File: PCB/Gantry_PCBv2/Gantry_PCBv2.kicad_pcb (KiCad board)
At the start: 2 copper layers, 190.5 x 121.8 mm, 168 parts, among them J1 Screw_Terminal_01x02, J10 B2B-XH-A_LF__SN_, J11 USB_C_Receptacle_USB2.0_16P, J12 Conn_01x04_Pin, J13 Conn_01x04_Pin, J14 Conn_01x04_Pin, J15 Conn_01x04_Pin, J16 Conn_01x05_Pin, J17 Conn_01x05_Pin, J2 DCJ200-10-A-XX-X_REVA, J3 Conn_01x03_Pin, J4 Conn_01x14, J5 B2B-XH-A_LF__SN_, J6 B2B-XH-A_LF__SN_, J7 B2B-XH-A_LF__SN_, J8 Conn_01x14, J9 Conn_01x10, Q1 NMOS, Q2 SS8050, Q3 SS8050, SW1 SW_0, SW2 SW_EN, SW3 SW_Push_DPDT, SW4 SW_Push_DPDT, U1 SN74CBT3244, U10 74HC245, U11 74HC245, U12 MCP23017_SO, U13 CP2102N-Axx-xQFN28, U14 ESP32-WROOM-32U, U2 MP1584, U4 TLV75733PDBV, U5 DRV8825_STEPPER_MOTOR_DRIVER_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, U6 DRV8825_STEPPER_MOTOR_DRIVER_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, U7 TB6612FNG H-bridge Motor Driv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, U8 DRV8825_STEPPER_MOTOR_DRIVER_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, U9 DRV8825_STEPPER_MOTOR_DRIVER_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

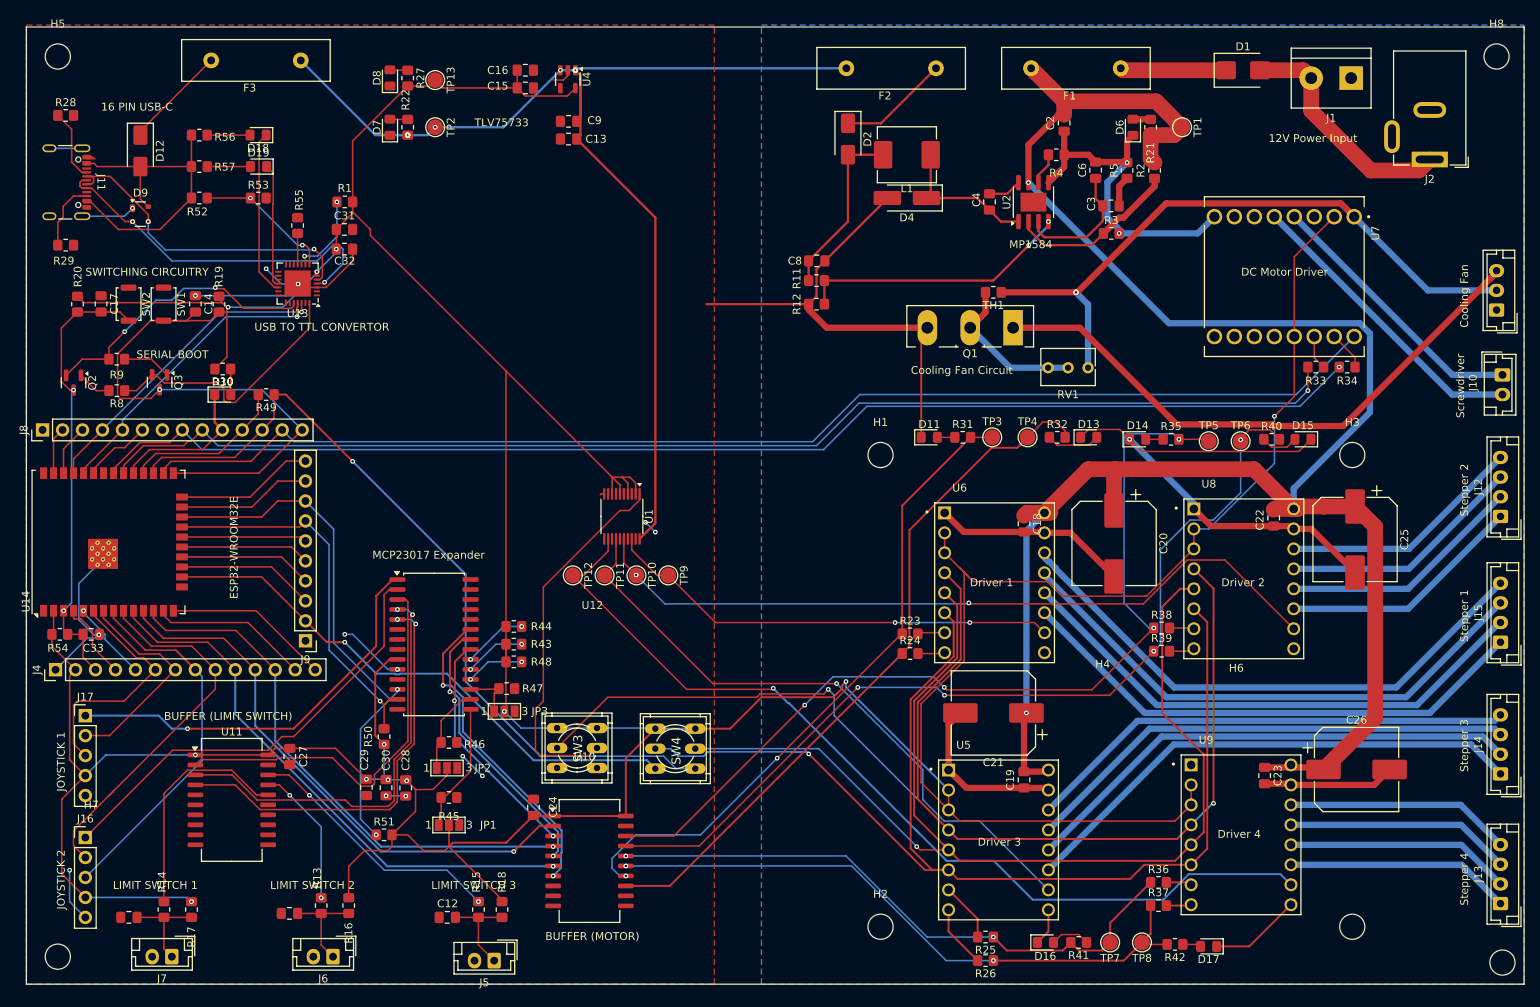
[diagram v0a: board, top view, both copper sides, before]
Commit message: Added Silkscreen
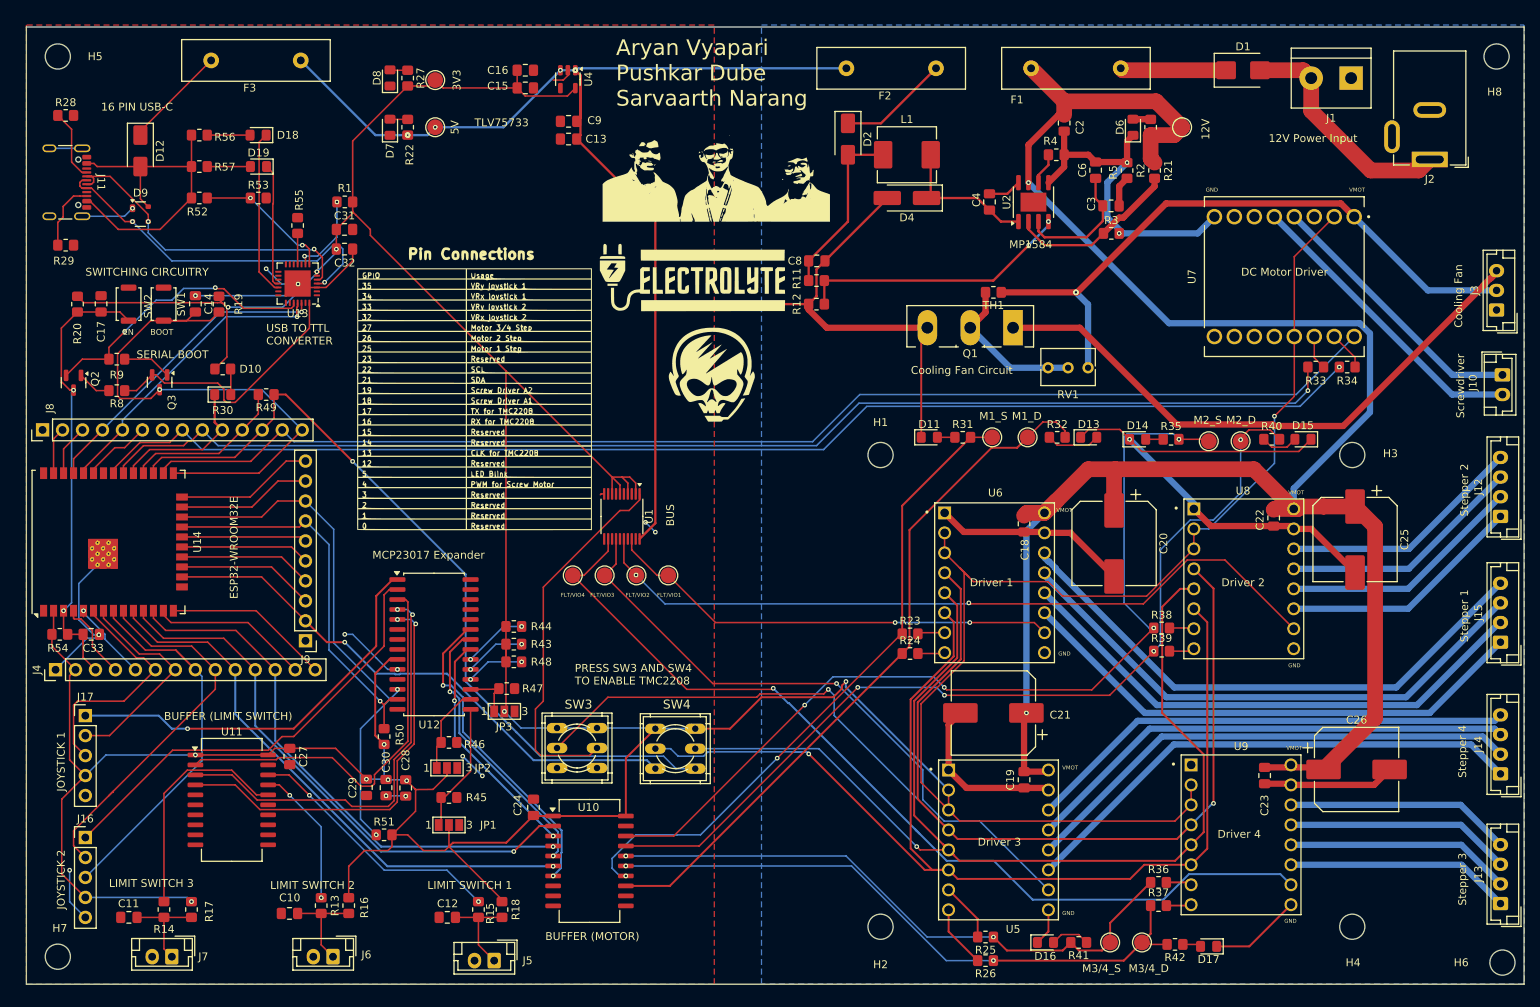
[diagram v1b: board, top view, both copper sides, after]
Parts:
- added G***: LOGO, Gantry:teamv3, F.Cu at (139.0, 41.4)
- added G***: LOGO, logos:sra_skull_big, F.Cu at (138.5, 68.0)
- added G***: LOGO, Gantry:logo, F.Cu at (135.8, 55.2)
- added G***: LOGO, Gantry:connectionsv2, F.Cu at (108.5, 69.3)
- renumbered TP1 to 12V, TP13 to 3V3, TP2 to 5V, TP9 to FLT/VIO1, TP10 to FLT/VIO2, TP11 to FLT/VIO3, TP12 to FLT/VIO4, TP4 to M1_D, TP3 to M1_S, TP6 to M2_D, TP5 to M2_S, TP8 to M3/4_D, TP7 to M3/4_S
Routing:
- net /12V_R: track 258.2 -> 259.6 mm
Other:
- board text added: "Aryan Vyapari Pushkar Dube Sarvaarth Narang"
- board text added: "BOOT"
- board text added: "BUS"
- board text added: "EN"
- board text added: "GND"
- board text added: "PRESS SW3 AND SW4 TO ENABLE TMC2208"
- board text added: "USB TO TTL CONVERTER"
- board text added: "VMOT"
- board text removed: "USB TO TTL CONVERTOR"

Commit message: FINAL ITERATION OF PCB, silkscreen complete
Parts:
- added G***: LOGO, Gantry:SRA_log, F.Cu at (141.2, 70.8)
- moved G*** 76.0 mm to (143.0, 130.9)
- moved G*** 37.7 mm to (108.5, 45.2)
- moved G*** 2.14 mm to (138.2, 43.4)
